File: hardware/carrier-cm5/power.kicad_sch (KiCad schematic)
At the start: 29 parts, among them IC203 TPS56A37RPAR, J10 XT30 VBAT, J11 J-SYSCTL

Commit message: cm5 carrier: io mcu sheet (elrs, lidar, lora, adc, buzzer) and gnss sheet
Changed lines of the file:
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@@
+		)
+	)
+	(hierarchical_label "VBAT"
+		(shape bidirectional)
+		(at 302.26 160.02 180)
+		(fields_autoplaced yes)
+		(effects
+			(font
+				(size 1.27 1.27)
+			)
+			(justify right)
+		)
+	)
+	(wire
+		(pts
+			(xy 302.26 160.02) (xy 312.42 160.02)
+		)
+		(stroke
+			(width 0)
+			(type default)
+		)
+	)
+	(label "VBAT"
+		(at 312.42 160.02 0)
+		(fields_autoplaced yes)
+		(effects
+			(font
+				(size 1.27 1.27)
+			)
+			(justify left bottom)
+		)
+	)
+	(hierarchical_label "NTC_SENSE"
+		(shape bidirectional)
+		(at 302.26 163.83 180)
+		(fields_autoplaced yes)
+		(effects
+			(font
+				(size 1.27 1.27)
+			)
+			(justify right)
+		)
+	)
+	(wire
+		(pts
+			(xy 302.26 163.83) (xy 312.42 163.83)
+		)
+		(stroke
+			(width 0)
+			(type default)
+		)
+	)
+	(label "NTC_SENSE"
+		(at 312.42 163.83 0)
+		(fields_autoplaced yes)
+		(effects
+			(font
+				(size 1.27 1.27)
+			)
+			(justify left bottom)
 		)
 	)

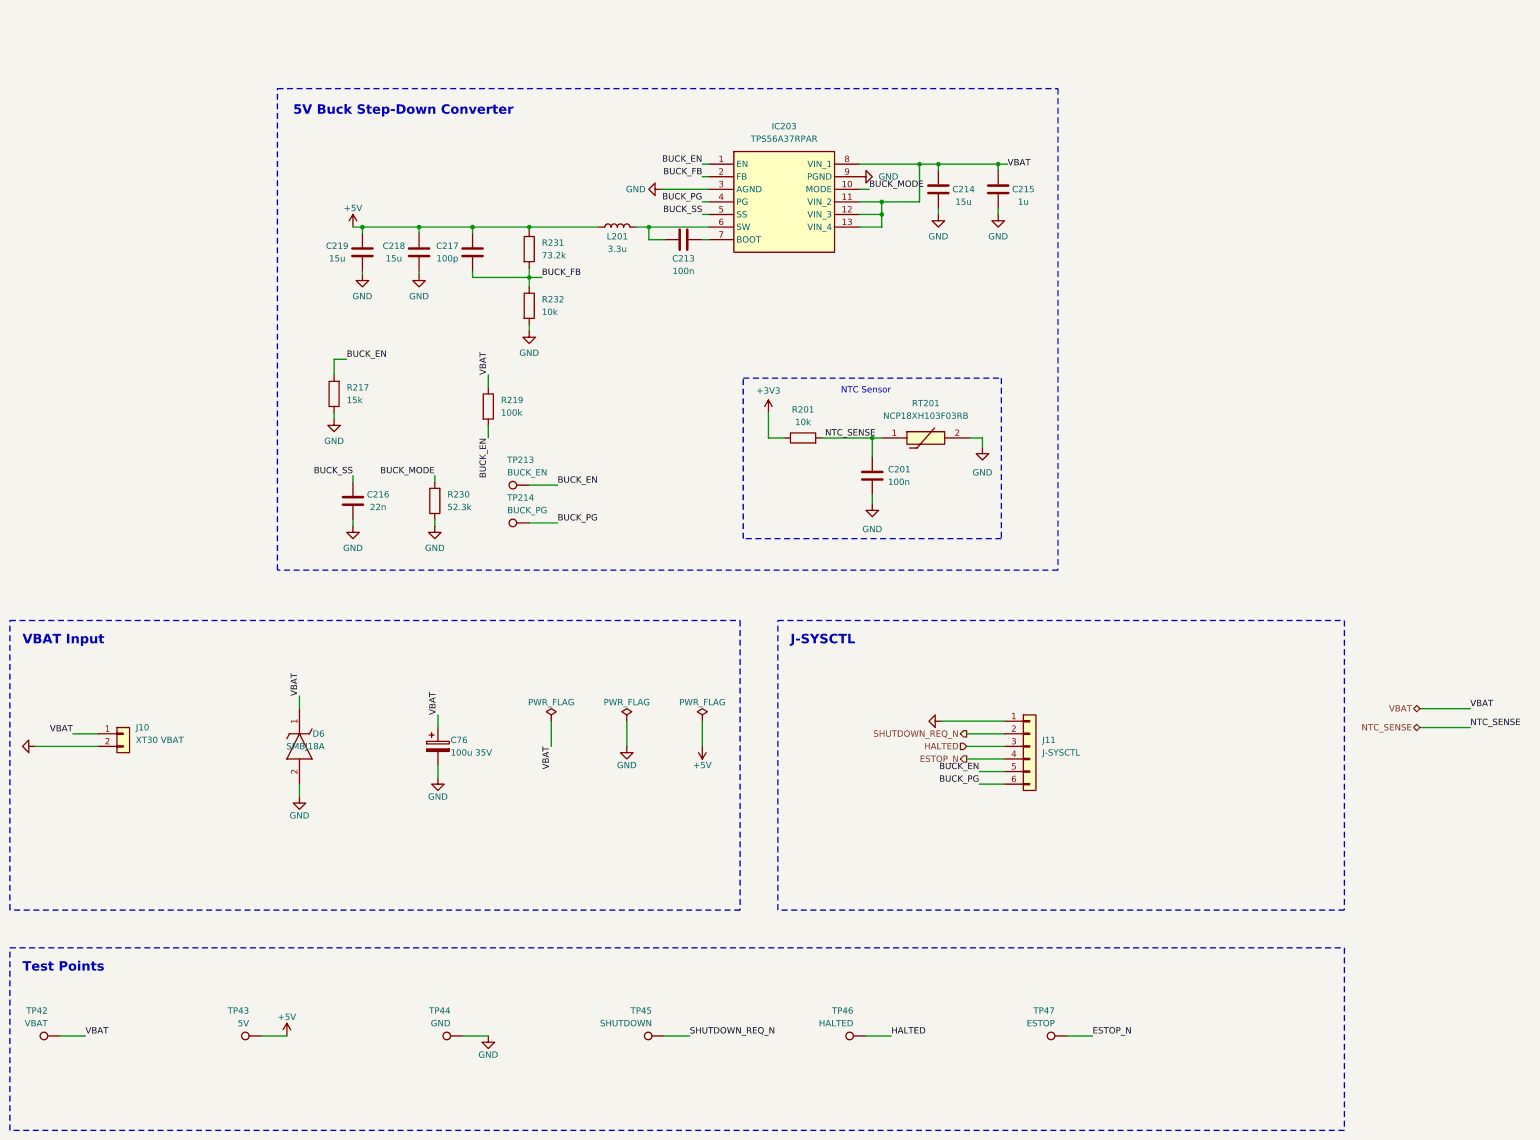
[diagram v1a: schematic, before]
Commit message: Updated schematic on CM5 carrier
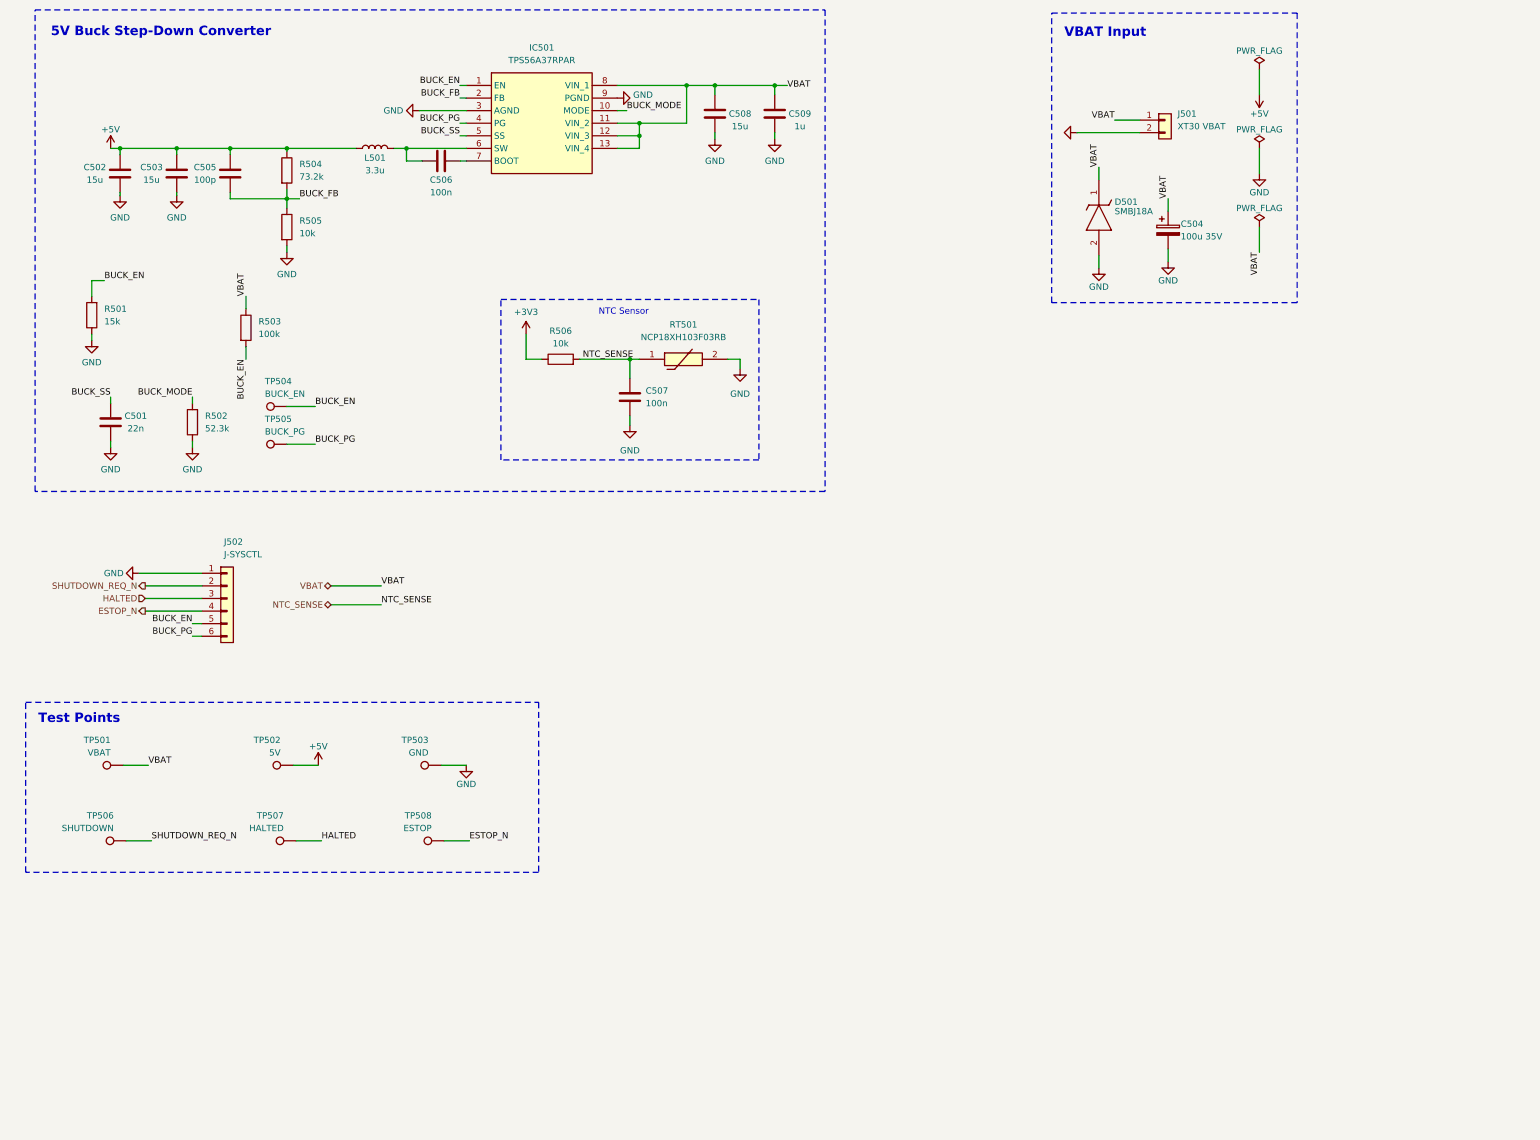
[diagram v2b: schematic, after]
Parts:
- renumbered C216 to C501, C219 to C502, C218 to C503, C76 to C504, C217 to C505, C213 to C506, C201 to C507, C214 to C508, C215 to C509, D6 to D501, IC203 to IC501, J10 to J501, J11 to J502, L201 to L501, R217 to R501, R230 to R502, R219 to R503, R231 to R504, R232 to R505, R201 to R506, RT201 to RT501, TP42 to TP501, TP43 to TP502, TP44 to TP503, TP213 to TP504, TP214 to TP505, TP45 to TP506, TP46 to TP507, TP47 to TP508
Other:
- note removed: "J-SYSCTL"
- company: AAC -> (none)
- moved on the sheet: C501, C502, C503, C504, C505, C506, C507, C508, C509, D501, IC501, J501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

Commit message: carrier: xh can and sysctl connectors, io mcu wiring tidy
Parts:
- J502: footprint Connector_JST:JST_GH_SM06B-GHS-TB_1x06-1MP_P1.25mm_Horizontal -> Connector_JST:JST_XH_S6B-XH-A-1_1x06_P2.50mm_Horizontal
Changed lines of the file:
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@@
 			)
 		)
-		(property "Footprint" "Connector_JST:JST_GH_SM06B-GHS-TB_1x06-1MP_P1.25mm_Horizontal"
+		(property "Footprint" "Connector_JST:JST_XH_S6B-XH-A-1_1x06_P2.50mm_Horizontal"
 			(at 61.595 137.795 0)
 			(hide yes)
